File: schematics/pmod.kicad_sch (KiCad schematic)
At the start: 13 parts, among them J11 PinSocket_2x6_P2.54mm_Drill1.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, J12 Screw_Terminal_01x02, J13 Screw_Terminal_01x02, J14 Screw_Terminal_01x03, J15 Screw_Terminal_01x04, J3 Screw_Terminal_01x02, J7 Screw_Terminal_01x02, U37 TPD4E05U06QDQARQ1, U38 TPD4E05U06QDQARQ1

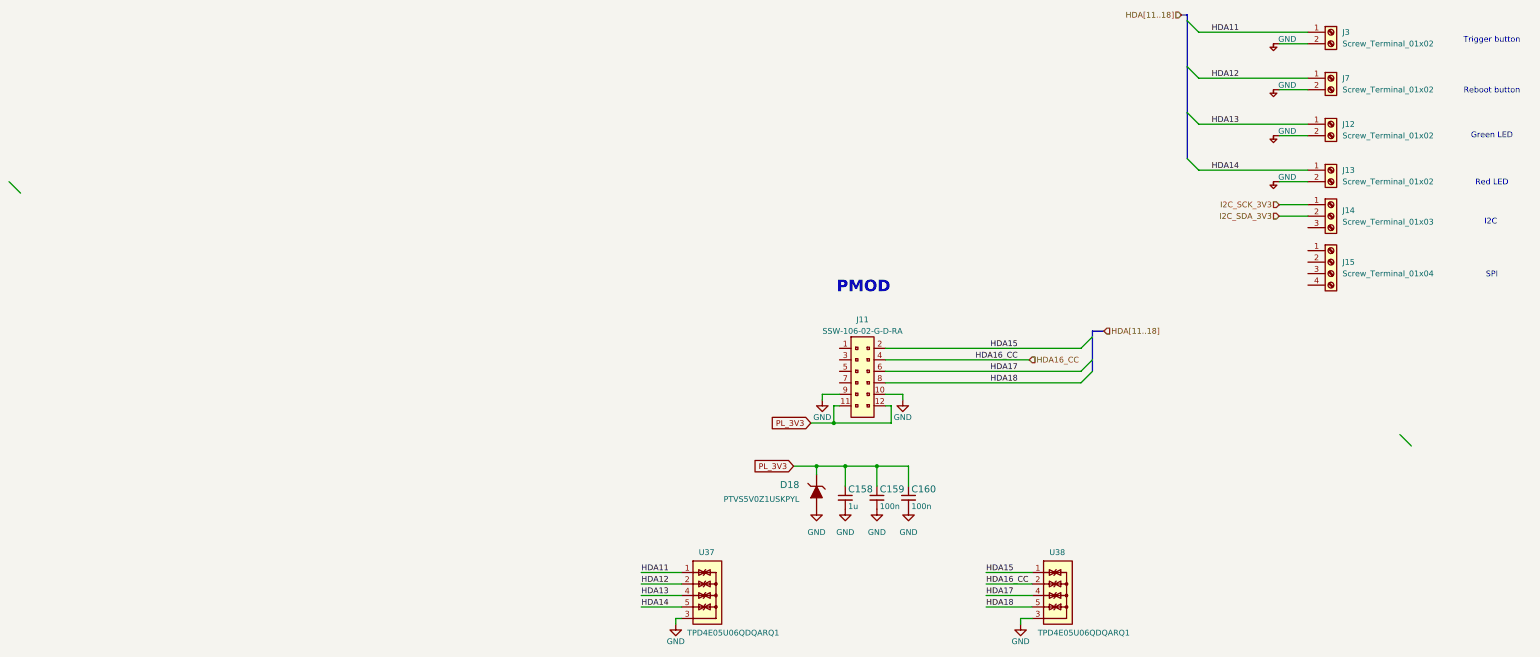
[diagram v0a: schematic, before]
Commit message: Voltage converter added
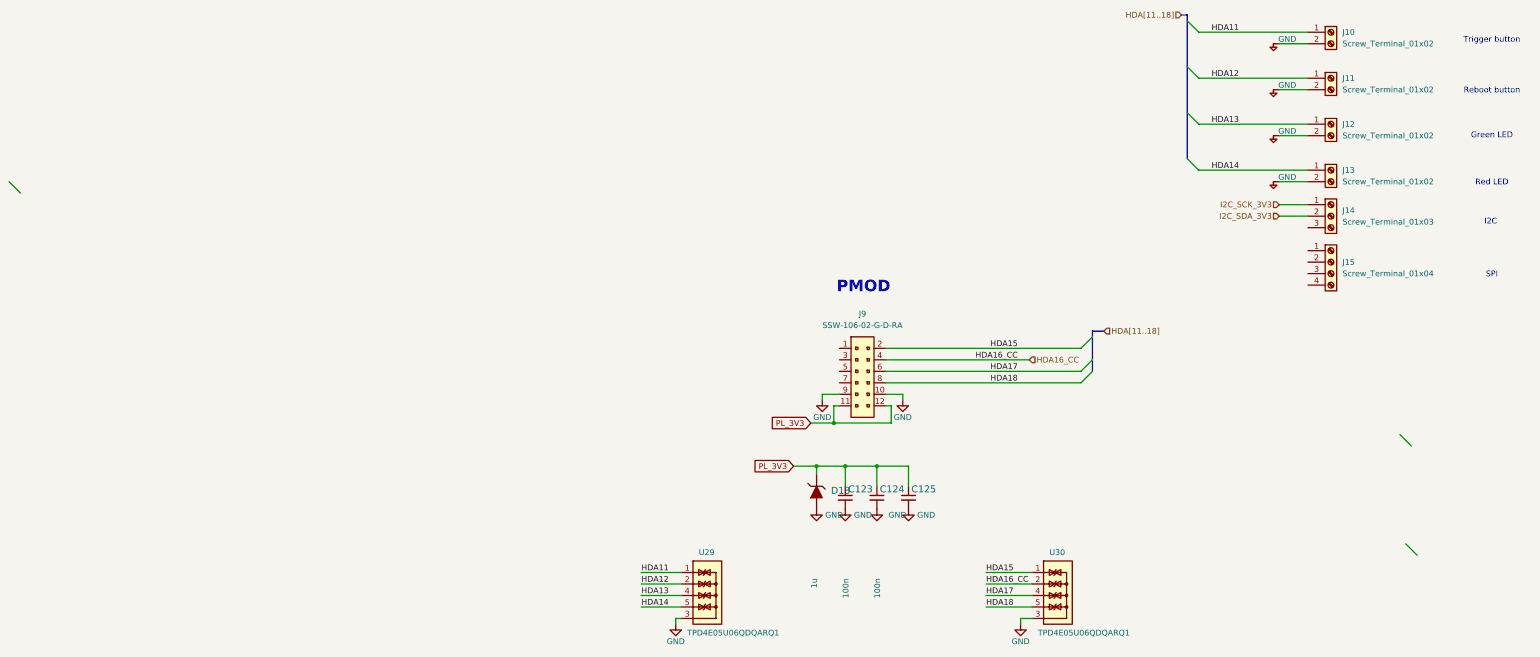
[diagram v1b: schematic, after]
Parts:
- J10: renamed from J3; footprint TerminalBlock_Phoenix:TerminalBlock_Phoenix_MPT-0,5-2-2.54_1x02_P2.54mm_Horizontal -> (none)
- J11: renamed from J7; footprint TerminalBlock_Phoenix:TerminalBlock_Phoenix_MPT-0,5-2-2.54_1x02_P2.54mm_Horizontal -> (none)
- J12, J13: footprint TerminalBlock_Phoenix:TerminalBlock_Phoenix_MPT-0,5-2-2.54_1x02_P2.54mm_Horizontal -> (none)
- J14: footprint TerminalBlock_Phoenix:TerminalBlock_Phoenix_MPT-0,5-3-2.54_1x03_P2.54mm_Horizontal -> (none)
- J15: footprint TerminalBlock_Phoenix:TerminalBlock_Phoenix_MPT-0,5-4-2.54_1x04_P2.54mm_Horizontal -> (none)
- renumbered C158 to C123, C159 to C124, C160 to C125, D18 to D13, J11 to J9, U37 to U29, U38 to U30
